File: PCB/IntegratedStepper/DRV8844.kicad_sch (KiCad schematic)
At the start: 21 parts, among them IC4 DRV8243HQRXYRQ1, IC5 DRV8243HQRXYRQ1

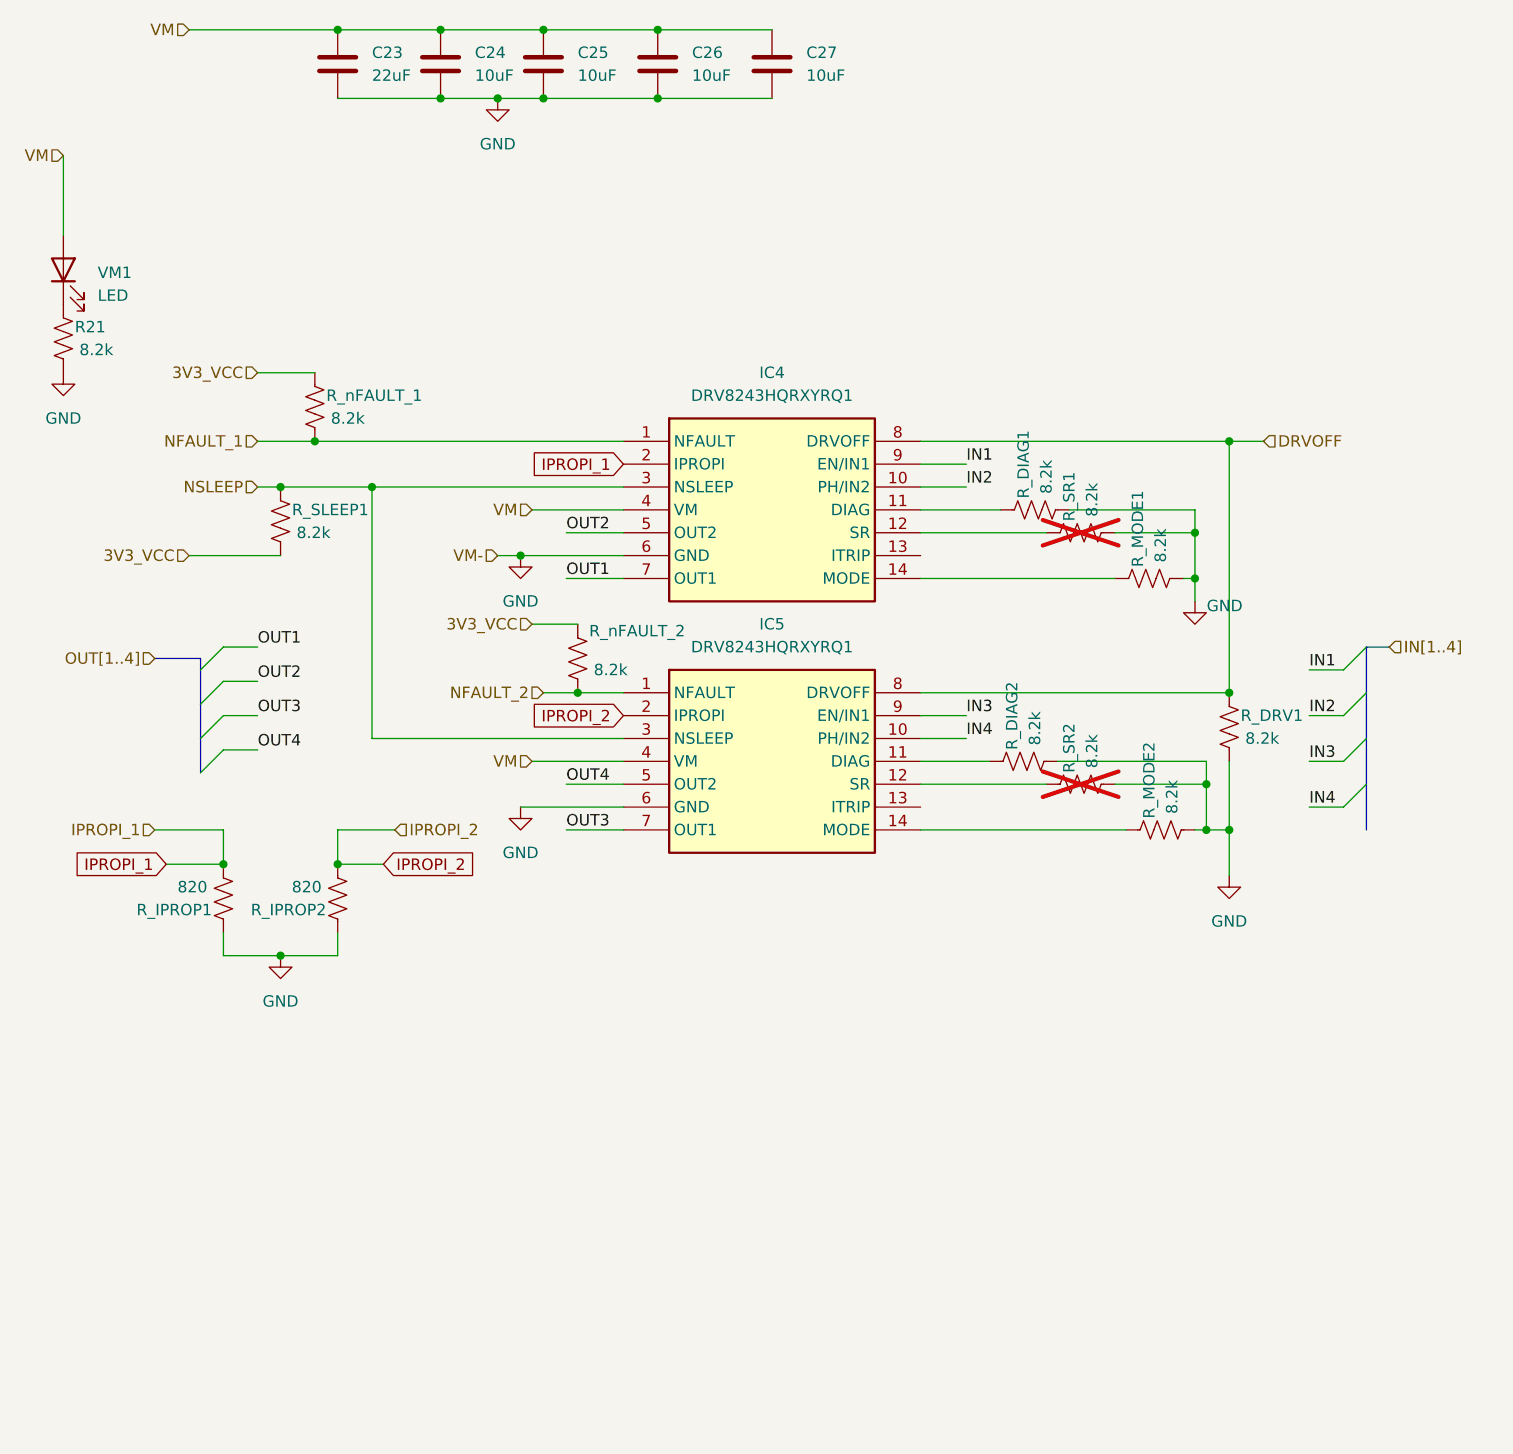
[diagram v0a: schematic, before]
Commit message: update new tester board sch
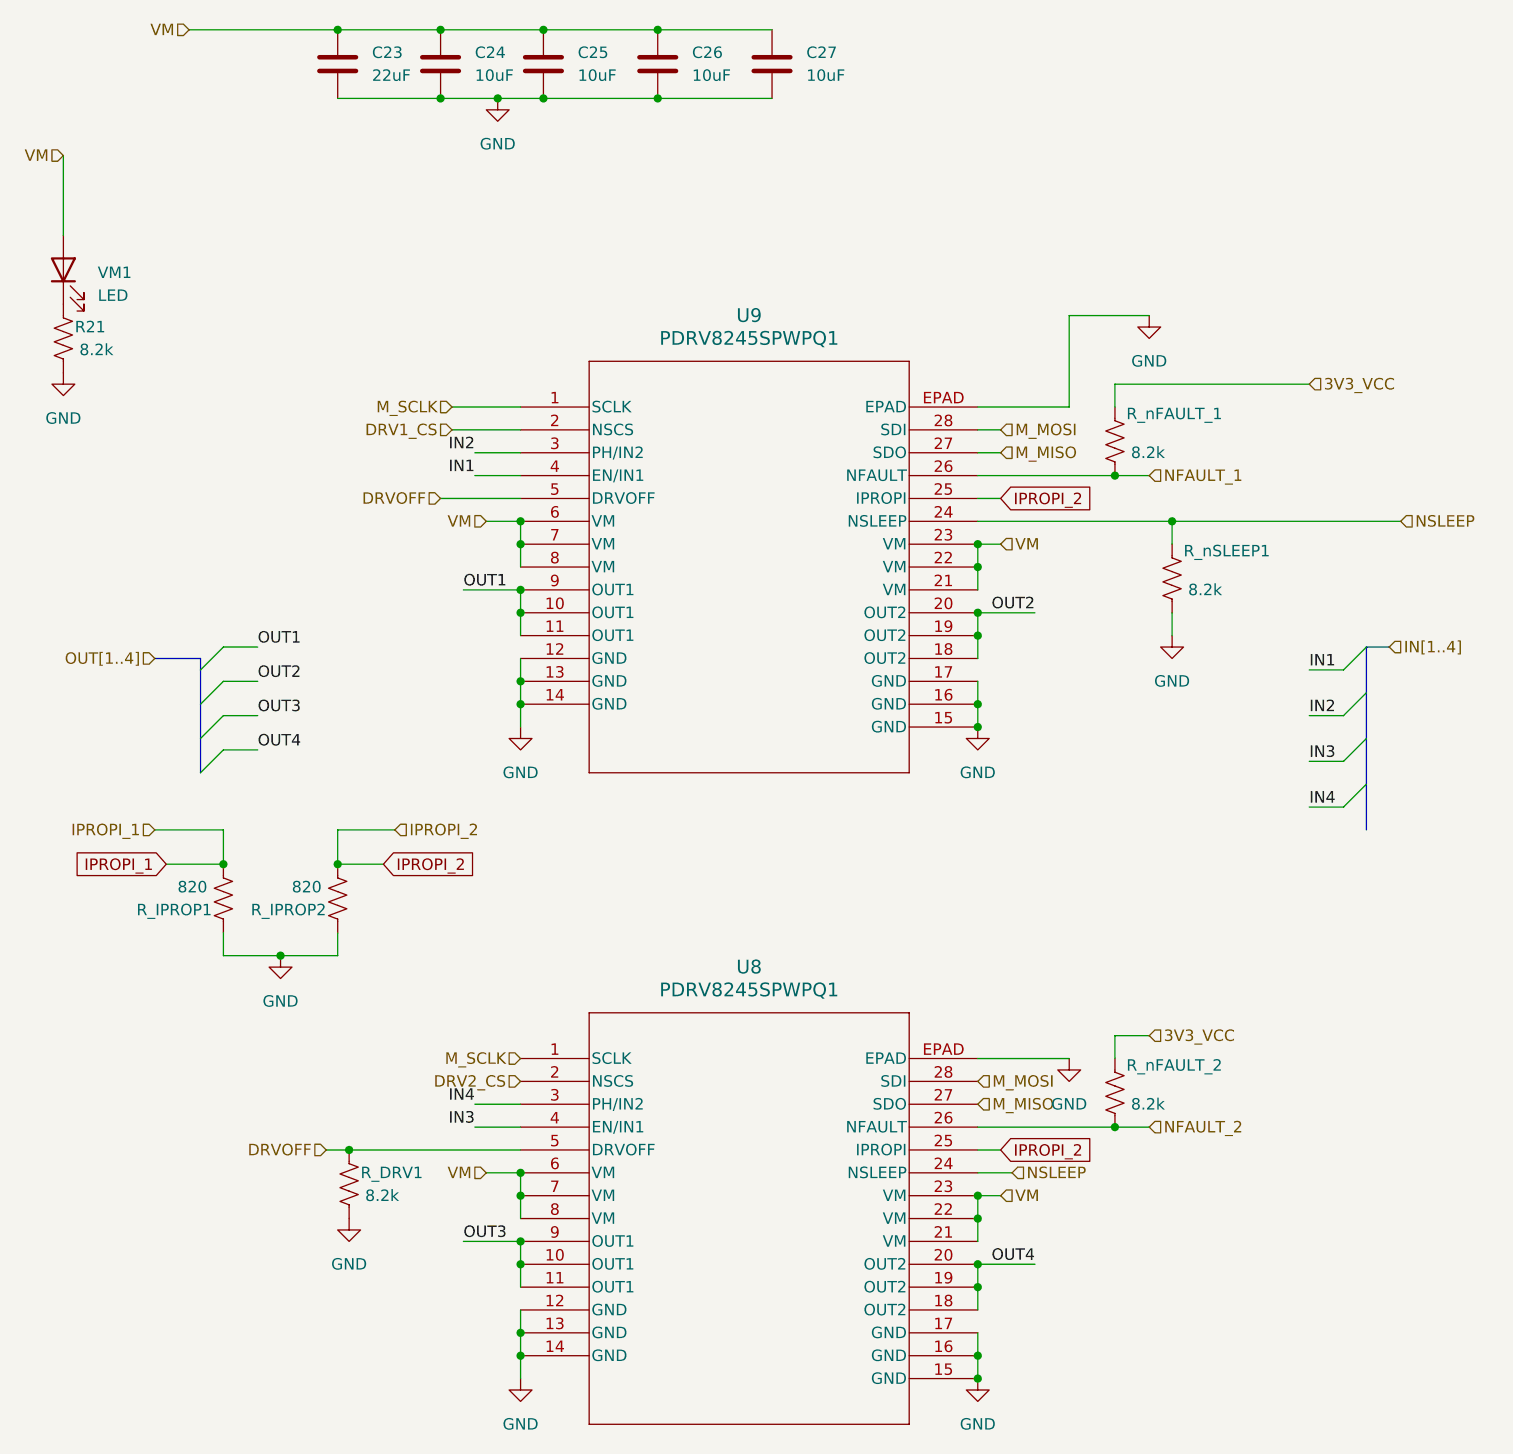
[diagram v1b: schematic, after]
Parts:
- removed IC4, IC5: DRV8243HQRXYRQ1, SamacSys_Parts:DRV8243HQRXYRQ1, symbol SamacSys_Parts:DRV8243HQRXYRQ1
- removed R_DIAG1, R_DIAG2, R_MODE1, R_MODE2, R_SLEEP1, R_SR1, R_SR2: 8.2k, Resistor_SMD:R_0603_1608Metric, symbol Device:R_US
- added R_nSLEEP1: 8.2k, Resistor_SMD:R_0603_1608Metric, symbol Device:R_US
- added U8, U9: PDRV8245SPWPQ1, U_PWP0028R_TEX, symbol PDRV8245SPWPQ1:PDRV8245SPWPQ1
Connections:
- net DRVOFF: now also U8.5 (DRVOFF), U9.5 (DRVOFF)
- net GND: now also R_nSLEEP1.1, U8.12 (GND), U8.13 (GND), U8.14 (GND), U8.15 (GND), U8.16 (GND), U8.17 (GND), U8.EPAD, U9.12 (GND), U9.13 (GND), U9.14 (GND), U9.15 (GND), U9.16 (GND), U9.17 (GND), U9.EPAD
- net IN1: now also U9.4 (EN/IN1)
- net IN2: now also U9.3 (PH/IN2)
- net IN3: now also U8.4 (EN/IN1)
- net IN4: now also U8.3 (PH/IN2)
- net IPROPI_2: now also U8.25 (IPROPI), U9.25 (IPROPI)
- net NFAULT_1: now also U9.26 (NFAULT)
- net NFAULT_2: now also U8.26 (NFAULT)
- net NSLEEP: now also R_nSLEEP1.2, U8.24 (NSLEEP), U9.24 (NSLEEP)
- net OUT1: now also U9.10 (OUT1), U9.11 (OUT1), U9.9 (OUT1)
- net OUT2: now also U9.18 (OUT2), U9.19 (OUT2), U9.20 (OUT2)
- net OUT3: now also U8.10 (OUT1), U8.11 (OUT1), U8.9 (OUT1)
- net OUT4: now also U8.18 (OUT2), U8.19 (OUT2), U8.20 (OUT2)
- net VM: now also U8.21 (VM), U8.22 (VM), U8.23 (VM), U8.6 (VM), U8.7 (VM), U8.8 (VM), U9.21 (VM), U9.22 (VM), U9.23 (VM), U9.6 (VM), U9.7 (VM), U9.8 (VM)
- new net DRV1_CS: U9.2 (NSCS)
- new net DRV2_CS: U8.2 (NSCS)
- new net M_MISO: U8.27 (SDO), U9.27 (SDO)
- new net M_MOSI: U8.28 (SDI), U9.28 (SDI)
- new net M_SCLK: U8.1 (SCLK), U9.1 (SCLK)

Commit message: update new layout with DRV8245
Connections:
- net IPROPI_1: now also U9.25 (IPROPI)
- net IPROPI_2: no longer U9.25 (IPROPI)
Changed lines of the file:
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@@
 		)
 	)
-	(global_label "IPROPI_2"
+	(global_label "IPROPI_1"
 		(shape input)
 		(at 166.37 81.28 0)
